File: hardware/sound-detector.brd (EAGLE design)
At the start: 43.2 x 22.9 mm, 38 parts, among them IC1 LMV324

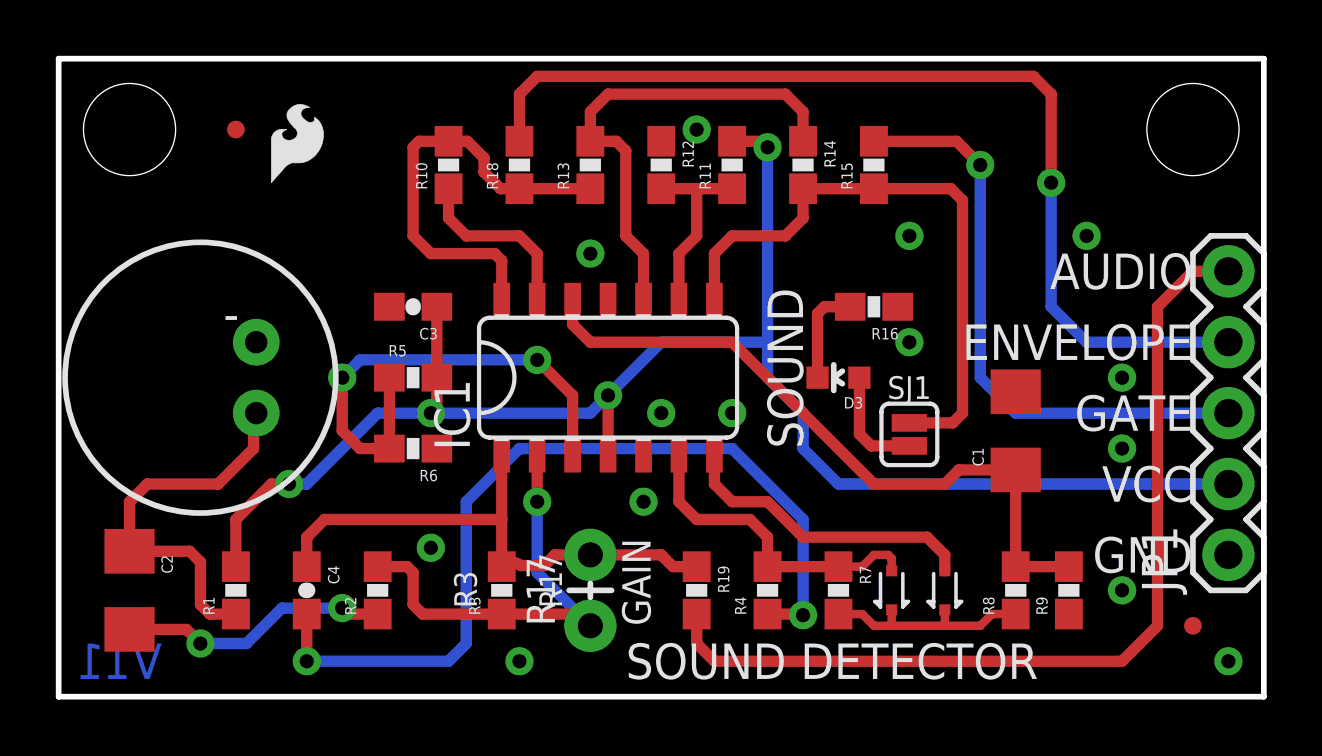
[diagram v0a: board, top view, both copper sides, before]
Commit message: changed fiducial from micro to regular
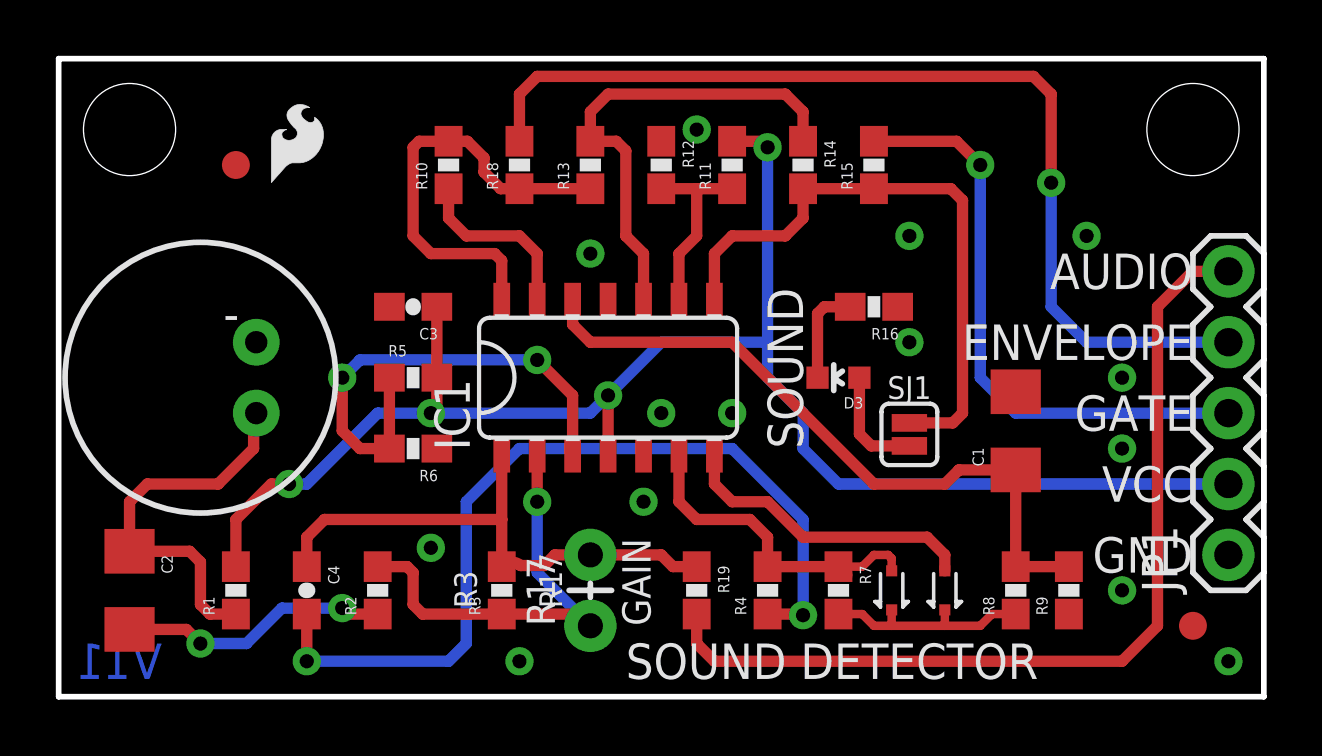
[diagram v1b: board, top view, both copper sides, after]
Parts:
- removed FID1, FID2: FIDUCIALUFIDUCIAL, SparkFun-Aesthetics:MICRO-FIDUCIAL
- added FID3, FID4: FIDUCIAL1X2, SparkFun-Aesthetics:FIDUCIAL-1X2
